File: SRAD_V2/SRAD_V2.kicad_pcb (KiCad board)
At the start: 4 copper layers, 76.2 x 152.4 mm, 143 parts, among them IC1 NCV81071BZR2G, IC2 NCV81071BZR2G, J1 Conn_01x04_Pin, J2 Conn_01x02_Pin, J3 RSP-122811-02, J4 USB_C_Receptacle_USB2.0_16P, J5 S02B-XASS-1LFSN, J7 S02B-XASS-1LFSN, M1 MountingHole_3.5mm_Pad, M2 MountingHole_3.5mm_Pad, M3 MountingHole_3.5mm_Pad, M4 MountingHole_3.5mm_Pad, Q1 NTMFS5C673NT1G, Q2 NTMFS5C673NT1G, Q3 NTMFS5C673NT1G, Q4 NTMFS5C673NT1G, Q6 MMBT3904LT3G, U1 STM32F767ZIT6, U12 MAX-M10S, U13 MS5607-02BA, U14 MMC5983MA, U17 AS5F31G04SND-08LIN, U2 TPS563200, U3 TMCS1108A2UQDR, U5 LSM6DSVTR, X1 Crystal

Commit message: Design for Aesthetics!
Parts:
- removed kibuzzard-6A3D76D6: G***, kibuzzard-6A3D76D6
- added kibuzzard-6A958C9B: G***, kibuzzard-6A958C9B, F.Cu at (107.6, 94.9)
- L1: footprint Inductor:IND_BOURNS_SRN8040 -> Inductor_SMD:L_Bourns_SRP5030T
- moved kibuzzard-6A84BD9F 3.68 mm to (83.5, 159.1)
- moved kibuzzard-6A3D75FD 2.86 mm to (123.1, 126.1)
- moved L1 2.40 mm to (119.1, 119.0)
- moved J2 2.14 mm to (127.6, 118.6)
- moved CR5 2.07 mm to (129.8, 126.5)
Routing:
- net Net-(U2-SW): track 8.66 -> 11.5 mm
- net GND: track 283.6 -> 285.2 mm, vias 200 -> 202
- net /Power Delivery System/+3.3V: track 24.2 -> 23.1 mm
- net +3.3V: track 493.3 -> 492.5 mm

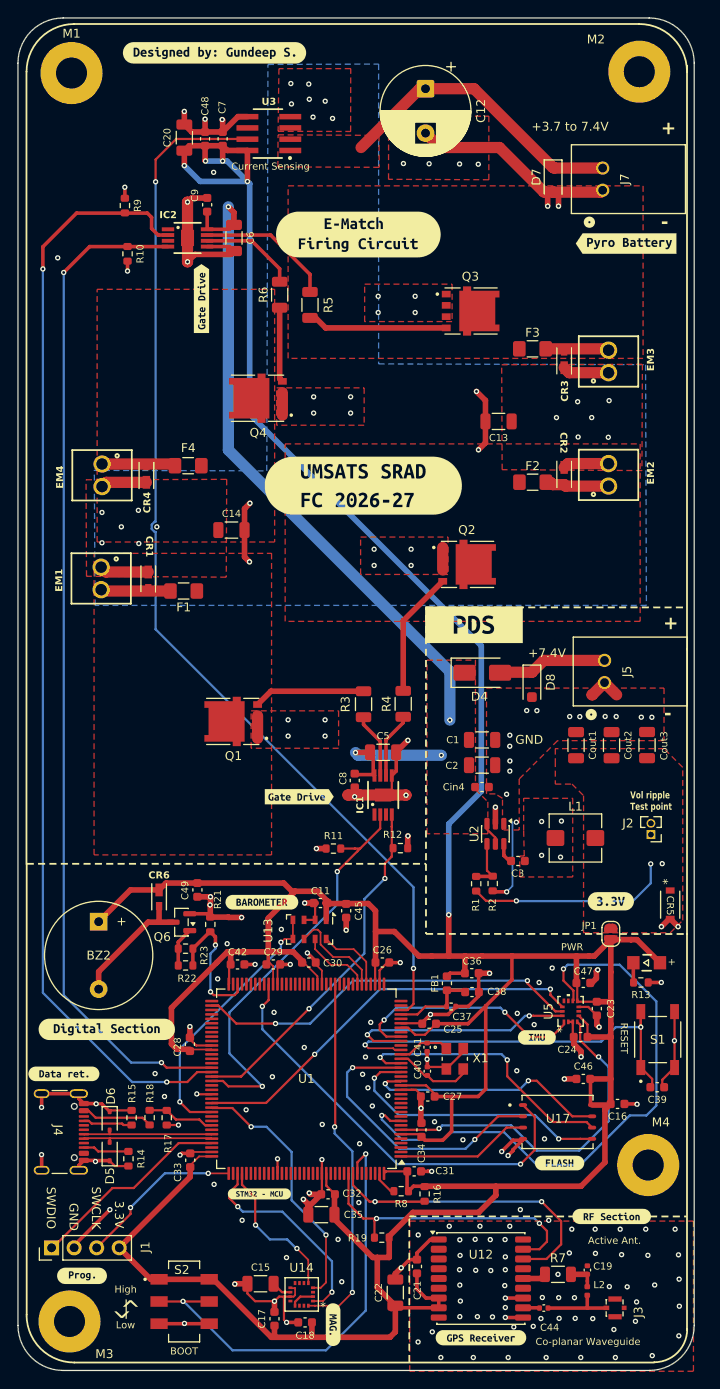
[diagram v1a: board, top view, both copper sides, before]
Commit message: optimised PDS layout by reducing loop area
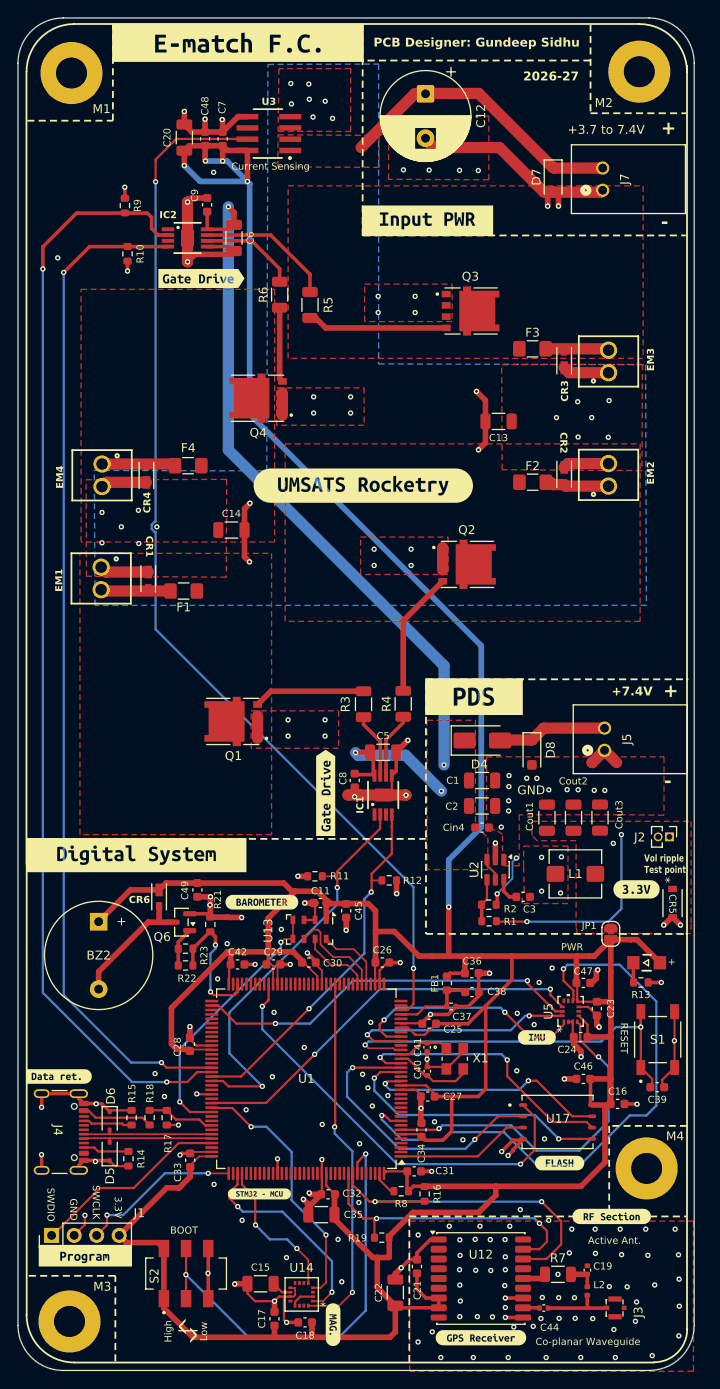
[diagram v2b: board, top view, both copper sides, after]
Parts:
- removed kibuzzard-6A876146: G***, kibuzzard-6A876146
- removed kibuzzard-6A8761B9: G***, kibuzzard-6A8761B9
- removed kibuzzard-6A8C3A39: G***, kibuzzard-6A8C3A39
- removed kibuzzard-6A905257: G***, kibuzzard-6A905257
- removed kibuzzard-6A9053B7: G***, kibuzzard-6A9053B7
- removed kibuzzard-6A905469: G***, kibuzzard-6A905469
- removed kibuzzard-6A90551E (x2): G***, kibuzzard-6A90551E
- removed kibuzzard-6A90556B: G***, kibuzzard-6A90556B
- added kibuzzard-6A95C150: G***, kibuzzard-6A95C150, F.Cu at (102.4, 49.4)
- added kibuzzard-6A95C1A9: G***, kibuzzard-6A95C1A9, F.Cu at (81.1, 29.3)
- added kibuzzard-6A95C5A9: G***, kibuzzard-6A95C5A9, F.Cu at (60.9, 145.8)
- added kibuzzard-6A95C804: G***, kibuzzard-6A95C804, F.Cu at (63.9, 166.0)
- added kibuzzard-6A95CBD7: G***, kibuzzard-6A95CBD7, F.Cu at (69.6, 120.9)
- added kibuzzard-6A95CC6E: G***, kibuzzard-6A95CC6E, F.Cu at (90.9, 113.9)
- added kibuzzard-6A95CC9C: G***, kibuzzard-6A95CC9C, F.Cu at (76.9, 55.9)
- added kibuzzard-6A95CD47: G***, kibuzzard-6A95CD47, F.Cu at (95.2, 79.2)
- moved Cout3 9.74 mm to (121.8, 116.7)
- moved Cout2 9.23 mm to (118.9, 116.7)
- moved Cout1 8.81 mm to (115.9, 116.7)
- moved kibuzzard-6A958C9B 8.10 mm to (107.6, 103.0)
- moved D4 7.63 mm to (108.6, 108.0)
- moved D8 7.63 mm to (114.2, 109.3)
- moved J5 7.63 mm to (122.4, 109.1)
- moved C2 4.60 mm to (108.6, 115.3)
- moved C1 4.57 mm to (108.6, 112.5)
- moved Cin4 4.57 mm to (108.5, 117.8)
- moved R1 4.46 mm to (109.3, 128.3), turned to 180 degrees
- moved C3 4.08 mm to (113.2, 125.6)
- moved L1 4.04 mm to (119.1, 123.0)
- moved U2 4.04 mm to (110.1, 122.5)
- moved R12 3.84 mm to (98.1, 123.7)
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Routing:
- net GND: track 285.2 -> 278.7 mm, vias 202 -> 201
- net +7.4VBATT: track 94.6 -> 101.1 mm
- net +3.3V: track 492.5 -> 497.0 mm
- net EM_CH2: track 39.9 -> 41.0 mm
- net Net-(U2-VFB): track 5.77 -> 4.93 mm
- net Net-(U2-VBST): track 2.37 -> 2.96 mm
- net SWDIO: track 22.9 -> 22.4 mm
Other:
- board text added: "2026-27"
- board text added: "PCB Designer: Gundeep Sidhu"

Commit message: Optimised PDS layout, among other small things
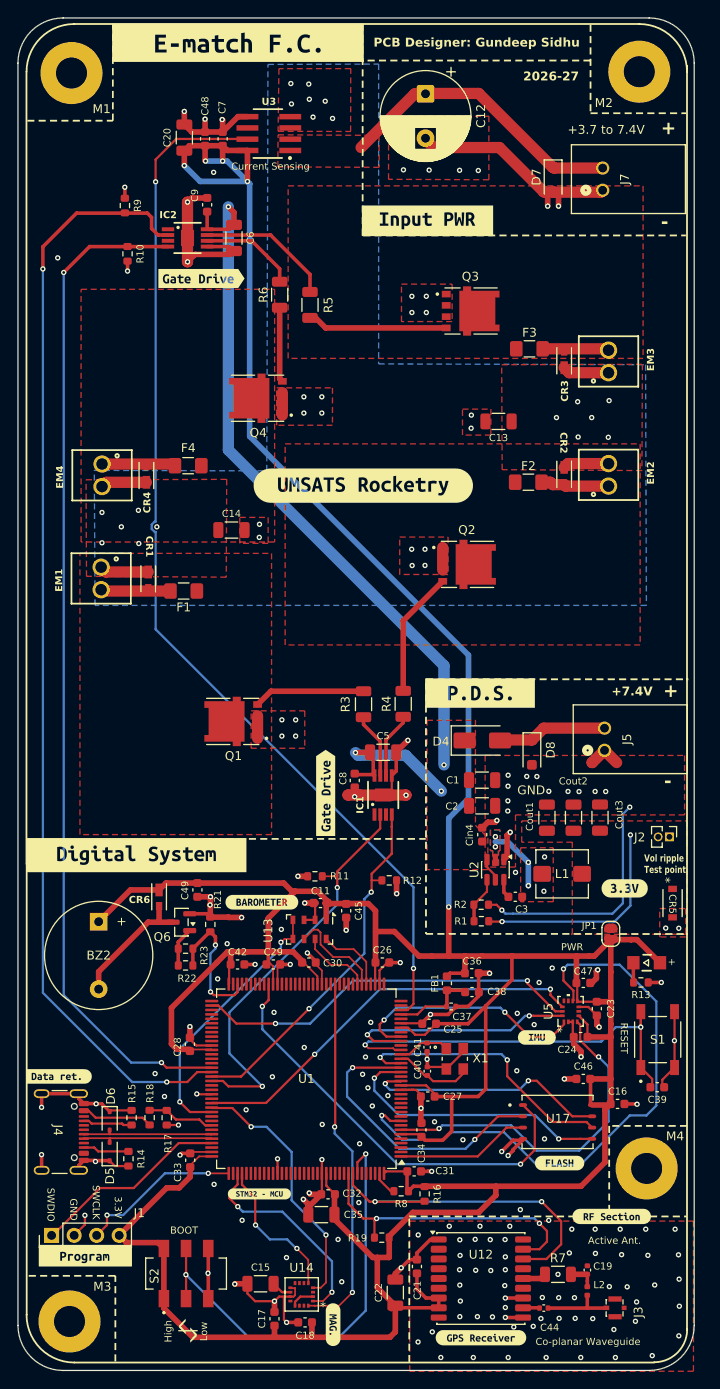
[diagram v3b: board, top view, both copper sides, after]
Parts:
- removed kibuzzard-6A958C9B: G***, kibuzzard-6A958C9B
- added kibuzzard-6A9704D1: G***, kibuzzard-6A9704D1, F.Cu at (108.3, 102.6)
- moved L1 1.50 mm to (117.6, 123.0)
- moved kibuzzard-6A3D75FD 1.34 mm to (124.6, 124.6)
- moved C3 0.88 mm to (112.3, 125.6)
- moved R1 0.86 mm to (108.5, 128.3)
- moved R2 0.86 mm to (108.5, 126.5)
- moved Cin4 0.80 mm to (108.6, 118.6), turned to 90 degrees
- moved F2 0.48 mm to (113.8, 78.9)
- moved F3 0.34 mm to (113.9, 63.8)
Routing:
- net GND: track 278.7 -> 288.0 mm, vias 201 -> 202
- net Net-(U2-SW): track 11.5 -> 7.31 mm, vias 3 -> 4
- net /Power Delivery System/+3.3V: track 23.1 -> 24.7 mm
- net +3.3V: track 497.0 -> 495.8 mm
- net Net-(U2-VBST): track 2.96 -> 2.13 mm
- added copper zone on B.Cu, net Net-(U2-SW)

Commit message: Designing proper via to via clearances for manufacturability
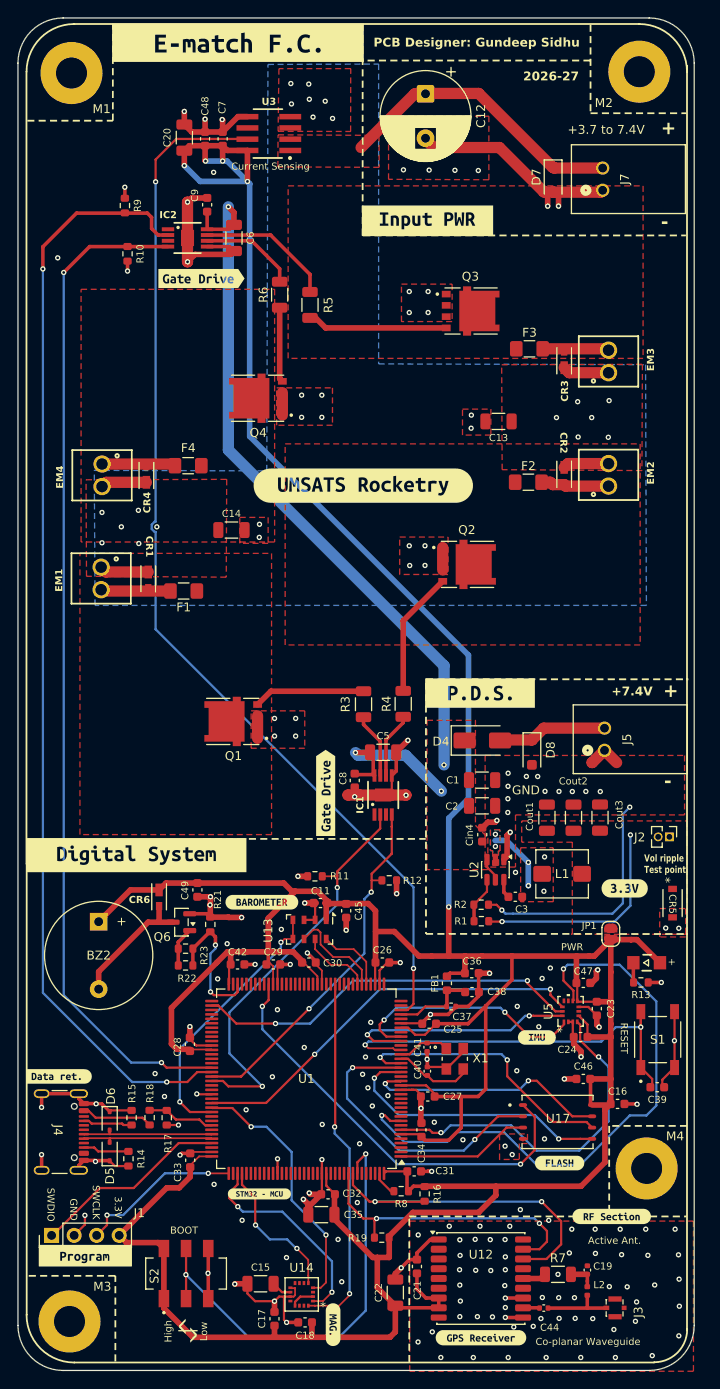
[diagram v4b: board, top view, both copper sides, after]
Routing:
- net GND: track 288.0 -> 282.5 mm
- net +3.3V: track 495.8 -> 497.6 mm

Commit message: Few layout adjustments
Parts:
- removed kibuzzard-6A8EFEDA: G***, kibuzzard-6A8EFEDA
- added LED1: WL-SMCW_1206, 150120SS75000:WL-SMCW_1206, F.Cu at (63.2, 142.0)
- added R20: 806R, Resistor_SMD:R_0603_1608Metric, F.Cu at (59.5, 141.4)
- added kibuzzard-6A982418: G***, kibuzzard-6A982418, F.Cu at (83.7, 126.2)
- D5, D6: value SD05C-01F -> STS321050B100
- D7, D8: value MBR1020VL -> SMF10CA
- moved kibuzzard-6A95C150 1.45 mm to (102.4, 48.0)
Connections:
- C44 pad 2: Net-(J3-SIGNAL) -> Net-(C44-Pad2)
- J3 pad 1: Net-(J3-SIGNAL) -> Net-(C44-Pad2)
- J3 pad 3: (no net) -> Net-(C44-Pad2)
- J3 pad 4: (no net) -> GND
- L2 pad 2: Net-(J3-SIGNAL) -> Net-(C44-Pad2)
- U1 pad 37: unconnected-(U1-PA3-Pad37) -> ADC1
- U1 pad 60: unconnected-(U1-PE9-Pad60) -> GPIO3
- U1 pad 80: unconnected-(U1-PD11-Pad80) -> Net-(U1-PD11)
- U1 pad 82: unconnected-(U1-PD13-Pad82) -> GPIO1
- U1 pad 85: unconnected-(U1-PD14-Pad85) -> GPS_FIX_LED
- U1 pad 93: unconnected-(U1-PG8-Pad93) -> GPIO2
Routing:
- net Net-(U1-PD11): track 0.00 -> 16.3 mm, vias 0 -> 2
- net Net-(C44-Pad2): track 0.00 -> 10.1 mm
- net Net-(J3-SIGNAL): track 8.05 -> 0.00 mm
- net Net-(LED1-Pad1): track 0.00 -> 2.32 mm
- net GND: track 282.5 -> 283.1 mm, vias 202 -> 204
- added copper zone on F.Cu, net USB_OTG_FS_D+
- added copper zone on F.Cu, net USB_OTG_FS_D-
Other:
- board text added: "- Giannis Georgiou"
- board text added: "- Heart Infinity"
- board text added: "- Ian Anderson"
- board text added: "- Summer Talon"
- board text added: "Special thanks to:"
- board text added: "V1.0"

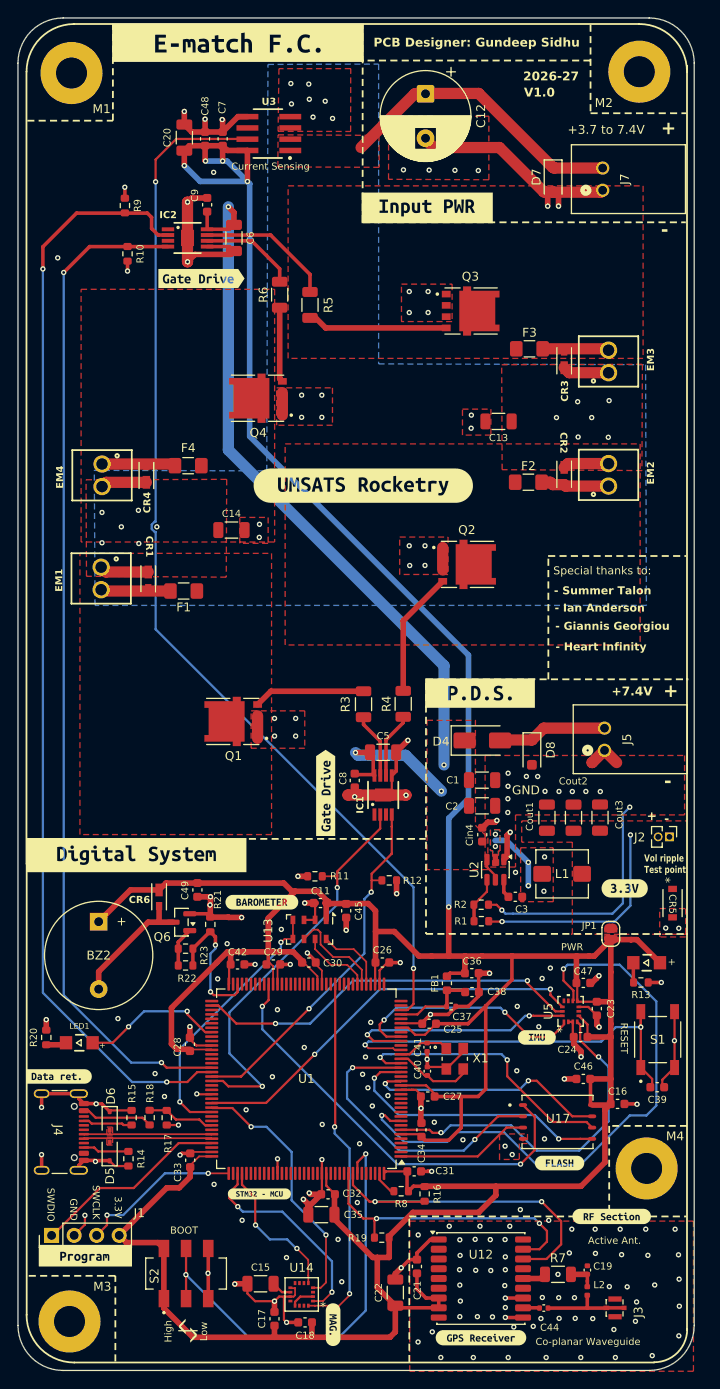
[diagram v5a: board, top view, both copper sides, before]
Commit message: Merged the new schematic with the main project successfully!
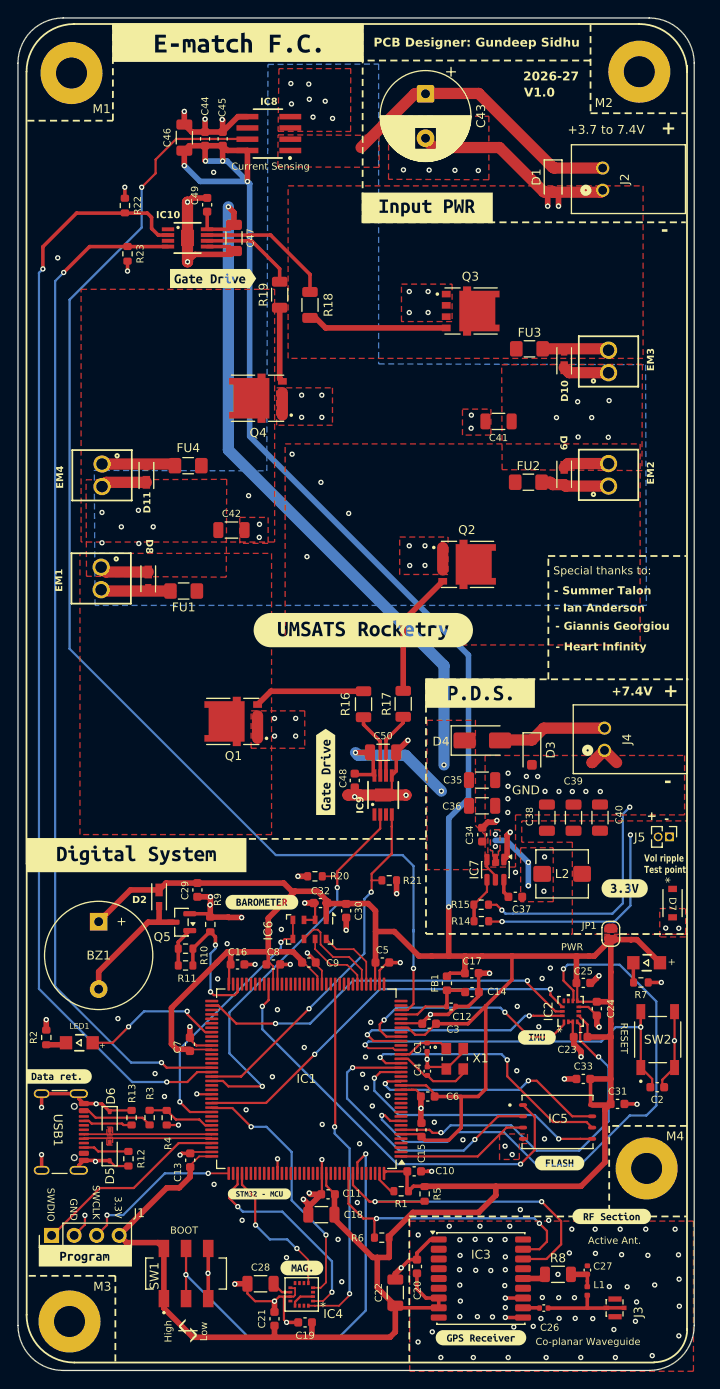
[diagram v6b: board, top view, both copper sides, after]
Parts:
- C1: renamed from C41; value 12p -> 12pF
- C12: renamed from C37; value 10n -> 10nF
- C14: renamed from C38; value 1u -> 1uF
- C17: renamed from C36; value 1u -> 1uF
- C18: renamed from C35; value 10u -> 10uF
- C19: renamed from C18; value 100n -> 100nF
- C20: renamed from C21; value 100n -> 100nF
- C21: renamed from C17; value 1u -> 1uF
- C22: value 10u -> 10uF
- C23: renamed from C24; value 100n -> 100nF
- C24: renamed from C23; value 100n -> 100nF
- C25: renamed from C47; value 1u -> 1uF
- C27: renamed from C19; value 10n -> 10nF
- C28: renamed from C15; value 10u -> 10uF
- C29: renamed from C49; value 1u -> 1uF
- C30: renamed from C45; value 1u -> 1uF
- C31: renamed from C16; value 100n -> 100nF
- C32: renamed from C11; value 100n -> 100nF
- C33: renamed from C46; value 1u -> 1uF
- C4: renamed from C40; value 12p -> 12pF
- C41: renamed from C13; value 10u -> 10uF
- C42: renamed from C14; value 10u -> 10uF
- C44: renamed from C48; value 1u -> 1uF
- C45: renamed from C7; value 100n -> 100nF
- C46: renamed from C20; value 10u -> 10uF
- C47: renamed from C6; value 10u -> 10uF
- C48: renamed from C8; value 100n -> 100nF
- C49: renamed from C9; value 100n -> 100nF
- C50: renamed from C5; value 10u -> 10uF
- L1: renamed from L2; value 27n -> 27nH
- moved kibuzzard-6A95CD47 16.3 mm to (95.2, 95.5)
- moved kibuzzard-6A876244 7.29 mm to (88.2, 167.4), turned to 0 degrees
- moved kibuzzard-6A95CC6E 2.37 mm to (90.9, 111.5)
- moved kibuzzard-6A95CC9C 1.31 mm to (78.2, 55.9)
- renumbered BZ2 to BZ1, C31 to C10, C32 to C11, C33 to C13, C34 to C15, C42 to C16, C39 to C2, C44 to C26, C25 to C3, Cin4 to C34, C1 to C35, C2 to C36, C3 to C37, Cout1 to C38, Cout2 to C39, Cout3 to C40, C12 to C43, C26 to C5, C27 to C6, C28 to C7, C29 to C8, C30 to C9, D7 to D1, CR3 to D10, CR4 to D11, CR6 to D2, D8 to D3, CR5 to D7, CR1 to D8, CR2 to D9, F1 to FU1, F2 to FU2, F3 to FU3, F4 to FU4, U1 to IC1, IC2 to IC10, U5 to IC2, U12 to IC3, U14 to IC4, U17 to IC5, U13 to IC6, U2 to IC7, U3 to IC8, IC1 to IC9, J7 to J2, J5 to J4, J2 to J5, L1 to L2, D1 to LED2, Q6 to Q5, R8 to R1, R23 to R10, R22 to R11, R14 to R12, R15 to R13, R1 to R14, R2 to R15, R3 to R16, R4 to R17, R5 to R18, R6 to R19, R20 to R2, R11 to R20, R12 to R21, R9 to R22, R10 to R23, R18 to R3, R17 to R4, R16 to R5, R19 to R6, R13 to R7, R7 to R8, R21 to R9, S2 to SW1, S1 to SW2, J4 to USB1
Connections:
- net /RF_IN renamed Net-(IC3-RF_IN)
- C26 pad 2: Net-(C44-Pad2) -> Net-(C26-Pad2)
- C41 pad 1: /E-match Firing Circuit/IN(-) -> Net-(C41-Pad1)
- IC8 pad 3: /E-match Firing Circuit/IN(-) -> Net-(C41-Pad1)
- L1 pad 2: Net-(C44-Pad2) -> Net-(C26-Pad2)
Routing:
- net I_VAL: track 120.7 -> 136.8 mm
- net EM_CH4: track 114.4 -> 115.2 mm
- net GND: vias 204 -> 209
